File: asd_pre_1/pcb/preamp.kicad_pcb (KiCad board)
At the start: 4 copper layers, 130 x 140 mm, 272 parts, among them P1 SD_Card_DM1, P10 LIN, P11 RIN, P12 LOUT, P13 ROUT, P14 MCU Debug, P15 FPGA Debug, P2 RJ45-MAGJACK, P3 TOSLINK, P4 SPDIF, P5 PwGnd, P6 GPIO, P7 Mute, P8 LEDs, P9 Volume, T1 S22083, U1 EFM32GG232F1024, U10 LM2937-12, U11 L79L12, U12 TPS54325, U13 TPS54294, U14 L78L05, U15 LM4562, U16 LM4562, U17 SD103ASDM, U18 SD103ASDM, U19 cs5361, U2 MAX3280E, U3 DIR9001, U4 CS4398, U5 LM4562, U6 ENC424J600, U7 N25Q128A, U8 oscillator, U9 xc7a100tftg256, X1 48MHz, X2 25MHz

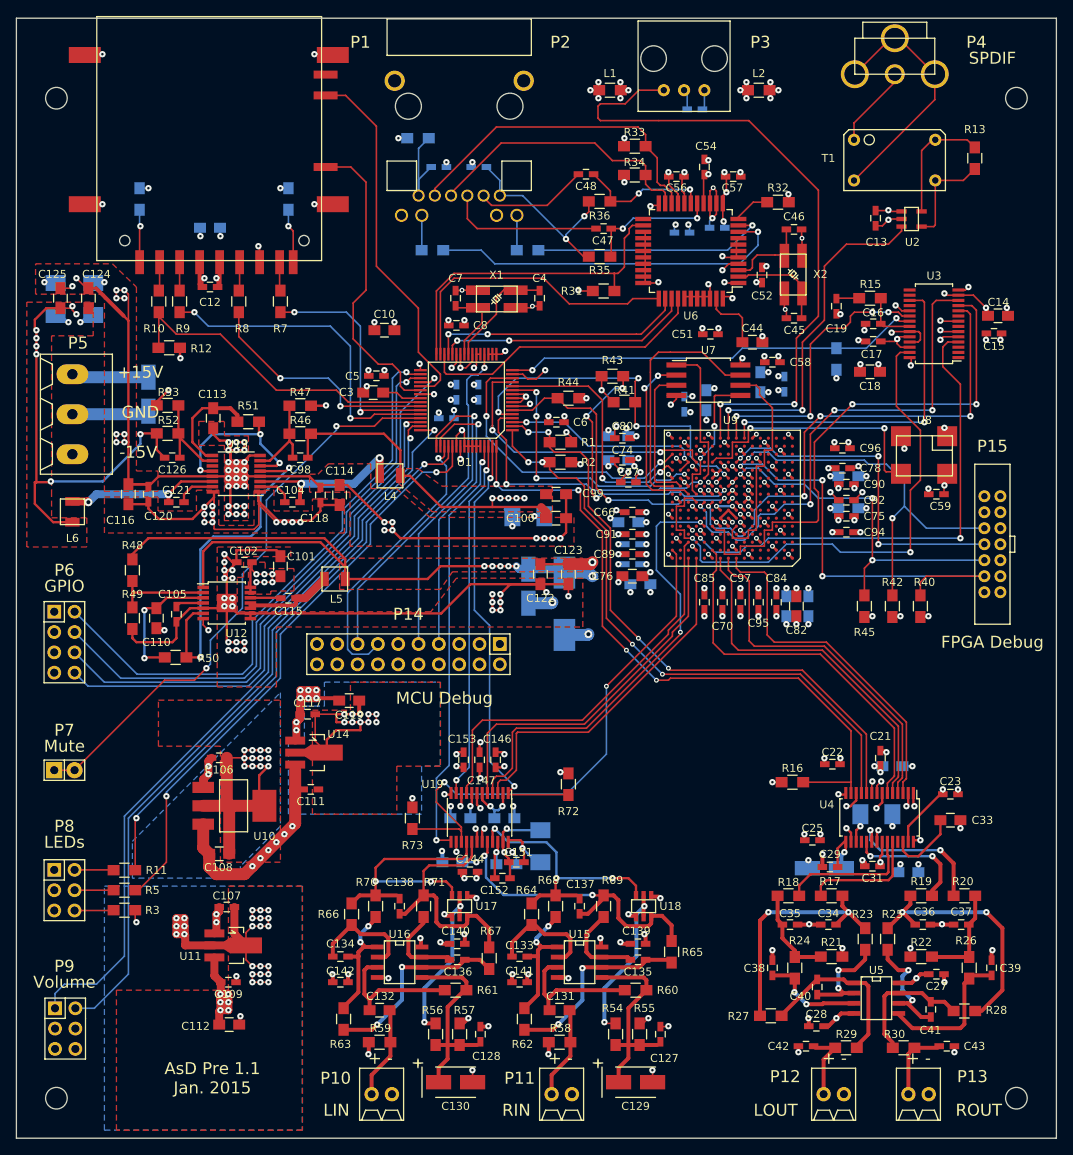
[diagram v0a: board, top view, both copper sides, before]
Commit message: Updated schematics and PCB.  Removed some minor errors with the first prototype.
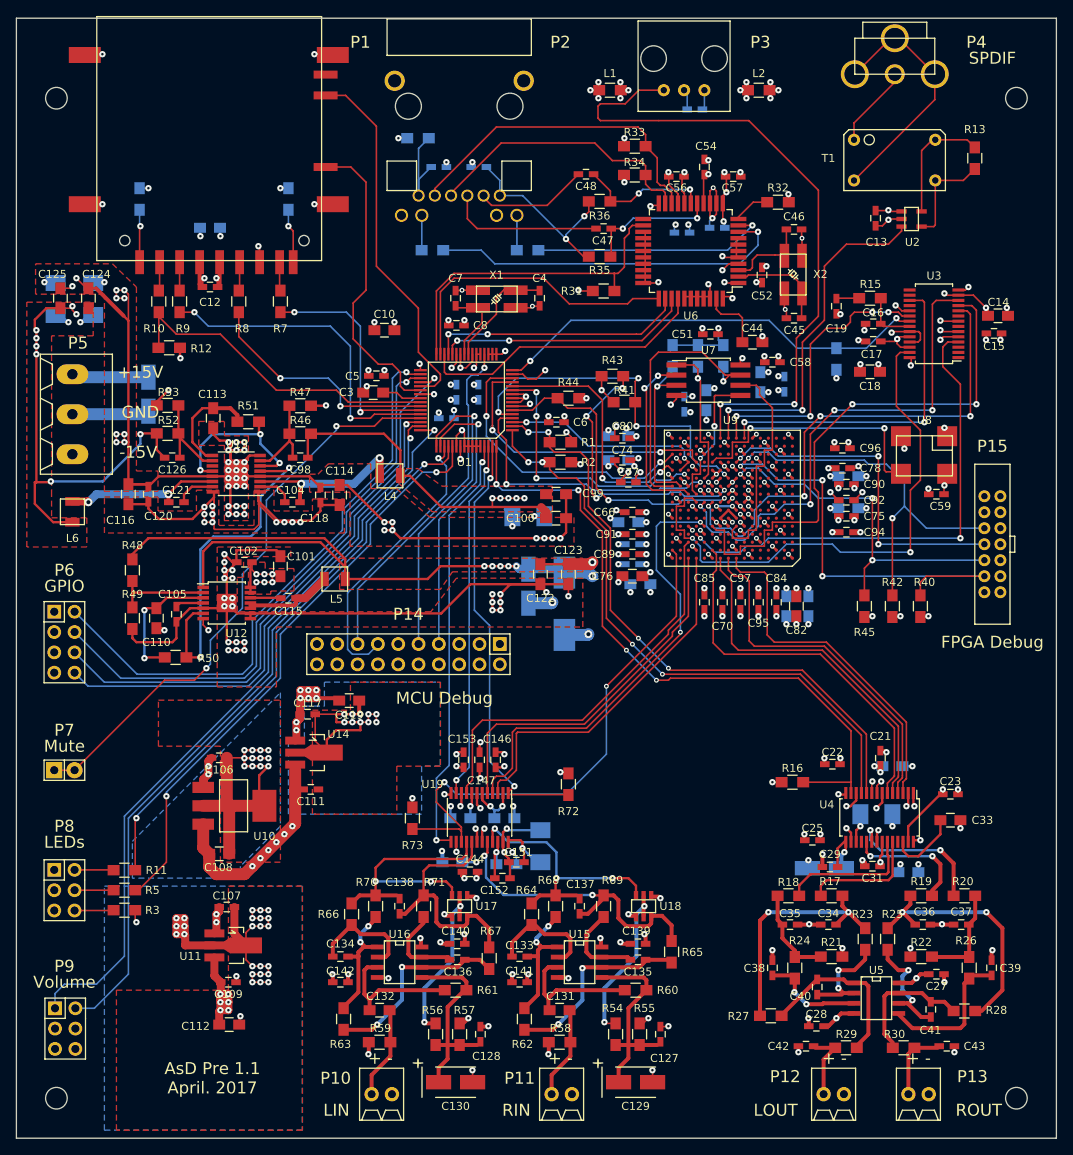
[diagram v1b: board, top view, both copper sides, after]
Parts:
- added R74: 2.4k, Resistors_SMD:R_0805_HandSoldering, B.Cu at (123.2, 69.2)
- added R75: 4.7k, Resistors_SMD:R_0805_HandSoldering, B.Cu at (120.0, 69.2)
- added R76: 4.7k, Resistors_SMD:R_0805_HandSoldering, B.Cu at (126.4, 69.2)
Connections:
- P1 pad 12: (no net) -> Net-(P1-Pad12)
- P14 pad 11: (no net) -> Net-(P14-Pad11)
- P14 pad 17: (no net) -> Net-(P14-Pad17)
- P14 pad 19: (no net) -> Net-(P14-Pad19)
- P14 pad 2: (no net) -> Net-(P14-Pad2)
- P14 pad 3: (no net) -> Net-(P14-Pad3)
- P14 pad 5: (no net) -> Net-(P14-Pad5)
- P15 pad 12: (no net) -> Net-(P15-Pad12)
- P15 pad 14: (no net) -> Net-(P15-Pad14)
- P9 pad 4: (no net) -> Net-(P9-Pad4)
- U13 pad 11: (no net) -> Net-(U13-Pad11)
- U3 pad 1: (no net) -> Net-(U3-Pad1)
- U3 pad 15: (no net) -> Net-(U3-Pad15)
- U3 pad 16: (no net) -> Net-(U3-Pad16)
- U3 pad 18: (no net) -> Net-(U3-Pad18)
- U3 pad 2: (no net) -> Net-(U3-Pad2)
- U3 pad 3: (no net) -> Net-(U3-Pad3)
- U3 pad 7: (no net) -> Net-(U3-Pad7)
- U3 pad 9: (no net) -> Net-(U3-Pad9)
- U4 pad 18: (no net) -> Net-(U4-Pad18)
- U4 pad 25: (no net) -> Net-(U4-Pad25)
- U6 pad 23: (no net) -> Net-(U6-Pad23)
- U9 pad A12: (no net) -> Net-(U9-PadA12)
- U9 pad A15: (no net) -> Net-(U9-PadA15)
- U9 pad A2: (no net) -> Net-(U9-PadA2)
- U9 pad A3: (no net) -> Net-(U9-PadA3)
- U9 pad A4: (no net) -> Net-(U9-PadA4)
- U9 pad A5: (no net) -> Net-(U9-PadA5)
- U9 pad A7: (no net) -> Net-(U9-PadA7)
- U9 pad B1: (no net) -> Net-(U9-PadB1)
- U9 pad B10: (no net) -> Net-(U9-PadB10)
- U9 pad B12: (no net) -> Net-(U9-PadB12)
- U9 pad B14: (no net) -> Net-(U9-PadB14)
- U9 pad B15: (no net) -> Net-(U9-PadB15)
- U9 pad B2: (no net) -> Net-(U9-PadB2)
- U9 pad B4: (no net) -> Net-(U9-PadB4)
- U9 pad B5: (no net) -> Net-(U9-PadB5)
- U9 pad B6: (no net) -> Net-(U9-PadB6)
- U9 pad B7: (no net) -> Net-(U9-PadB7)
- U9 pad B9: (no net) -> Net-(U9-PadB9)
- U9 pad C1: (no net) -> Net-(U9-PadC1)
- U9 pad C11: (no net) -> Net-(U9-PadC11)
- U9 pad C12: (no net) -> Net-(U9-PadC12)
- U9 pad C13: (no net) -> Net-(U9-PadC13)
- U9 pad C16: (no net) -> Net-(U9-PadC16)
- U9 pad C2: (no net) -> Net-(U9-PadC2)
- U9 pad C3: (no net) -> Net-(U9-PadC3)
- U9 pad C4: (no net) -> Net-(U9-PadC4)
- U9 pad C6: (no net) -> Net-(U9-PadC6)
- U9 pad C7: (no net) -> Net-(U9-PadC7)
- U9 pad C8: (no net) -> Net-(U9-PadC8)
- U9 pad C9: (no net) -> Net-(U9-PadC9)
- U9 pad D1: (no net) -> Net-(U9-PadD1)
- U9 pad D10: (no net) -> Net-(U9-PadD10)
- U9 pad D11: (no net) -> Net-(U9-PadD11)
- U9 pad D14: (no net) -> Net-(U9-PadD14)
- U9 pad D15: (no net) -> Net-(U9-PadD15)
- U9 pad D16: (no net) -> Net-(U9-PadD16)
- U9 pad D3: (no net) -> Net-(U9-PadD3)
- U9 pad D4: (no net) -> Net-(U9-PadD4)
- U9 pad D5: (no net) -> Net-(U9-PadD5)
- U9 pad D6: (no net) -> Net-(U9-PadD6)
- U9 pad D8: (no net) -> Net-(U9-PadD8)
- U9 pad D9: (no net) -> Net-(U9-PadD9)
- U9 pad E1: (no net) -> Net-(U9-PadE1)
- U9 pad E13: (no net) -> Net-(U9-PadE13)
- U9 pad E15: (no net) -> Net-(U9-PadE15)
- U9 pad E16: (no net) -> Net-(U9-PadE16)
- U9 pad E2: (no net) -> Net-(U9-PadE2)
- U9 pad E3: (no net) -> Net-(U9-PadE3)
- U9 pad E5: (no net) -> Net-(U9-PadE5)
- U9 pad E6: (no net) -> Net-(U9-PadE6)
- U9 pad F12: (no net) -> Net-(U9-PadF12)
- U9 pad F13: (no net) -> Net-(U9-PadF13)
- U9 pad F14: (no net) -> Net-(U9-PadF14)
- U9 pad F15: (no net) -> Net-(U9-PadF15)
- U9 pad F2: (no net) -> Net-(U9-PadF2)
- U9 pad F3: (no net) -> Net-(U9-PadF3)
- U9 pad F4: (no net) -> Net-(U9-PadF4)
- U9 pad F5: (no net) -> Net-(U9-PadF5)
- U9 pad G1: (no net) -> Net-(U9-PadG1)
- U9 pad G11: (no net) -> Net-(U9-PadG11)
- U9 pad G12: (no net) -> Net-(U9-PadG12)
- U9 pad G14: (no net) -> Net-(U9-PadG14)
- U9 pad G15: (no net) -> Net-(U9-PadG15)
- U9 pad G16: (no net) -> Net-(U9-PadG16)
- U9 pad G2: (no net) -> Net-(U9-PadG2)
- U9 pad G4: (no net) -> Net-(U9-PadG4)
- U9 pad G5: (no net) -> Net-(U9-PadG5)
- U9 pad H1: (no net) -> Net-(U9-PadH1)
- U9 pad H14: (no net) -> Net-(U9-PadH14)
- U9 pad H16: (no net) -> Net-(U9-PadH16)
- U9 pad H2: (no net) -> Net-(U9-PadH2)
- U9 pad H3: (no net) -> Net-(U9-PadH3)
- U9 pad H4: (no net) -> Net-(U9-PadH4)
- U9 pad H5: (no net) -> Net-(U9-PadH5)
- U9 pad J1: (no net) -> Net-(U9-PadJ1)
- U9 pad J15: (no net) -> Net-(U9-PadJ15)
- U9 pad J16: (no net) -> Net-(U9-PadJ16)
- U9 pad J3: (no net) -> Net-(U9-PadJ3)
- U9 pad J4: (no net) -> Net-(U9-PadJ4)
- U9 pad J5: (no net) -> Net-(U9-PadJ5)
- U9 pad K1: (no net) -> Net-(U9-PadK1)
- U9 pad K12: (no net) -> Net-(U9-PadK12)
- U9 pad K2: (no net) -> Net-(U9-PadK2)
- U9 pad K3: (no net) -> Net-(U9-PadK3)
- U9 pad K5: (no net) -> Net-(U9-PadK5)
- U9 pad K7: (no net) -> Net-(U9-PadK7)
- U9 pad K8: (no net) -> Net-(U9-PadK8)
- U9 pad L13: (no net) -> Net-(U9-PadL13)
- U9 pad L2: (no net) -> Net-(U9-PadL2)
- U9 pad L3: (no net) -> Net-(U9-PadL3)
- U9 pad L4: (no net) -> Net-(U9-PadL4)
- U9 pad L5: (no net) -> Net-(U9-PadL5)
- U9 pad M1: (no net) -> Net-(U9-PadM1)
- U9 pad M12: (no net) -> Net-(U9-PadM12)
- U9 pad M14: (no net) -> Net-(U9-PadM14)
- U9 pad M2: (no net) -> Net-(U9-PadM2)
- U9 pad M4: (no net) -> Net-(U9-PadM4)
- U9 pad M5: (no net) -> Net-(U9-PadM5)
- U9 pad M6: (no net) -> Net-(U9-PadM6)
- U9 pad N1: (no net) -> Net-(U9-PadN1)
- U9 pad N12: (no net) -> Net-(U9-PadN12)
- U9 pad N16: (no net) -> Net-(U9-PadN16)
- U9 pad N2: (no net) -> Net-(U9-PadN2)
- U9 pad N3: (no net) -> Net-(U9-PadN3)
- U9 pad N4: (no net) -> Net-(U9-PadN4)
- U9 pad N6: (no net) -> Net-(U9-PadN6)
- U9 pad N9: (no net) -> Net-(U9-PadN9)
- U9 pad P1: (no net) -> Net-(U9-PadP1)
- U9 pad P10: (no net) -> Net-(U9-PadP10)
- U9 pad P11: (no net) -> Net-(U9-PadP11)
- U9 pad P13: (no net) -> Net-(U9-PadP13)
- U9 pad P14: (no net) -> Net-(U9-PadP14)
- U9 pad P15: (no net) -> Net-(U9-PadP15)
- U9 pad P3: (no net) -> Net-(U9-PadP3)
- U9 pad P4: (no net) -> Net-(U9-PadP4)
- U9 pad P5: (no net) -> Net-(U9-PadP5)
- U9 pad P6: (no net) -> Net-(U9-PadP6)
- U9 pad P8: (no net) -> Net-(U9-PadP8)
- U9 pad P9: (no net) -> Net-(U9-PadP9)
- U9 pad R1: (no net) -> Net-(U9-PadR1)
- U9 pad R10: (no net) -> Net-(U9-PadR10)
- U9 pad R11: (no net) -> Net-(U9-PadR11)
- U9 pad R12: (no net) -> Net-(U9-PadR12)
- U9 pad R13: (no net) -> Net-(U9-PadR13)
- U9 pad R15: (no net) -> Net-(U9-PadR15)
- U9 pad R16: (no net) -> Net-(U9-PadR16)
- U9 pad R2: (no net) -> Net-(U9-PadR2)
- U9 pad R3: (no net) -> Net-(U9-PadR3)
- U9 pad R5: (no net) -> Net-(U9-PadR5)
- U9 pad R6: (no net) -> Net-(U9-PadR6)
- U9 pad R7: (no net) -> Net-(U9-PadR7)
- U9 pad R8: (no net) -> Net-(U9-PadR8)
- U9 pad T12: (no net) -> Net-(U9-PadT12)
- U9 pad T13: (no net) -> Net-(U9-PadT13)
- U9 pad T14: (no net) -> Net-(U9-PadT14)
- U9 pad T15: (no net) -> Net-(U9-PadT15)
- U9 pad T2: (no net) -> Net-(U9-PadT2)
- U9 pad T3: (no net) -> Net-(U9-PadT3)
- U9 pad T4: (no net) -> Net-(U9-PadT4)
- U9 pad T5: (no net) -> Net-(U9-PadT5)
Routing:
- net +3.3V: track 329.7 -> 338.5 mm
- net Net-(R76-Pad2): track 30.7 -> 35.0 mm, vias 0 -> 1
- net Net-(R75-Pad2): track 18.1 -> 21.1 mm, vias 0 -> 1
- net /SPDIF/nRST: track 52.7 -> 55.6 mm
- net Net-(R74-Pad2): track 17.8 -> 19.3 mm, vias 0 -> 1
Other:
- board text added: "AsD Pre 1.1 April. 2017"
- board text removed: "AsD Pre 1.1 Jan. 2015"
